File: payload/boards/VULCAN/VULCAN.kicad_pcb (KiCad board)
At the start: 2 copper layers, 63.5 x 101.6 mm, 78 parts, among them IC1 LT1001CS8#PBF, J1 XT60PW-M, J2 POWER, J3 I2C, J4 Serial, J5 SPI, J6 GPIO, J7 Screw_Terminal_01x06, J8 Screw_Terminal_01x06, U1 AZ1117IH-5.0TRG1, U2 DS18B20, U3 MAX31850KATB+T, U4 AP63357, U5 DEV-16771, U6 MAX31850KATB+T, U7 MAX31850KATB+T, U8 MAX31850KATB+T

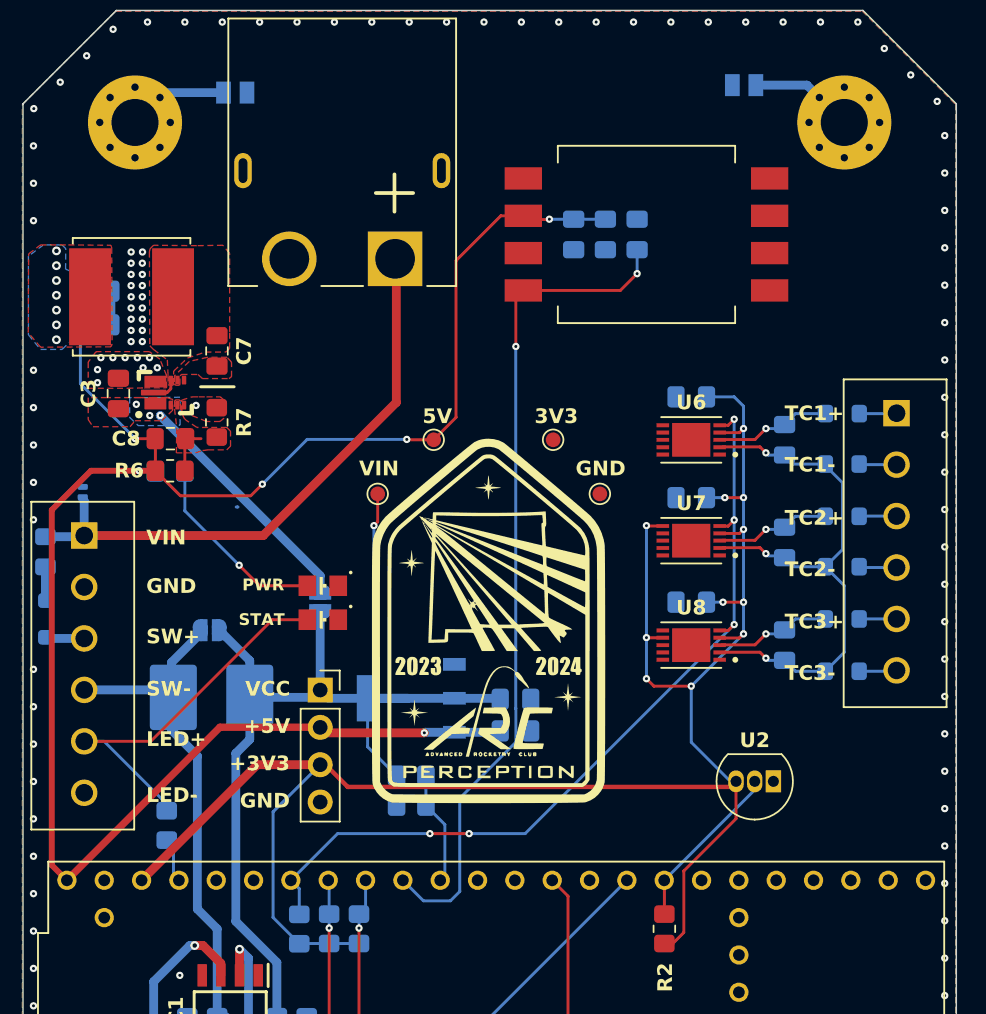
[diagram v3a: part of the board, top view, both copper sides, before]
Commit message: added ESD to TCs
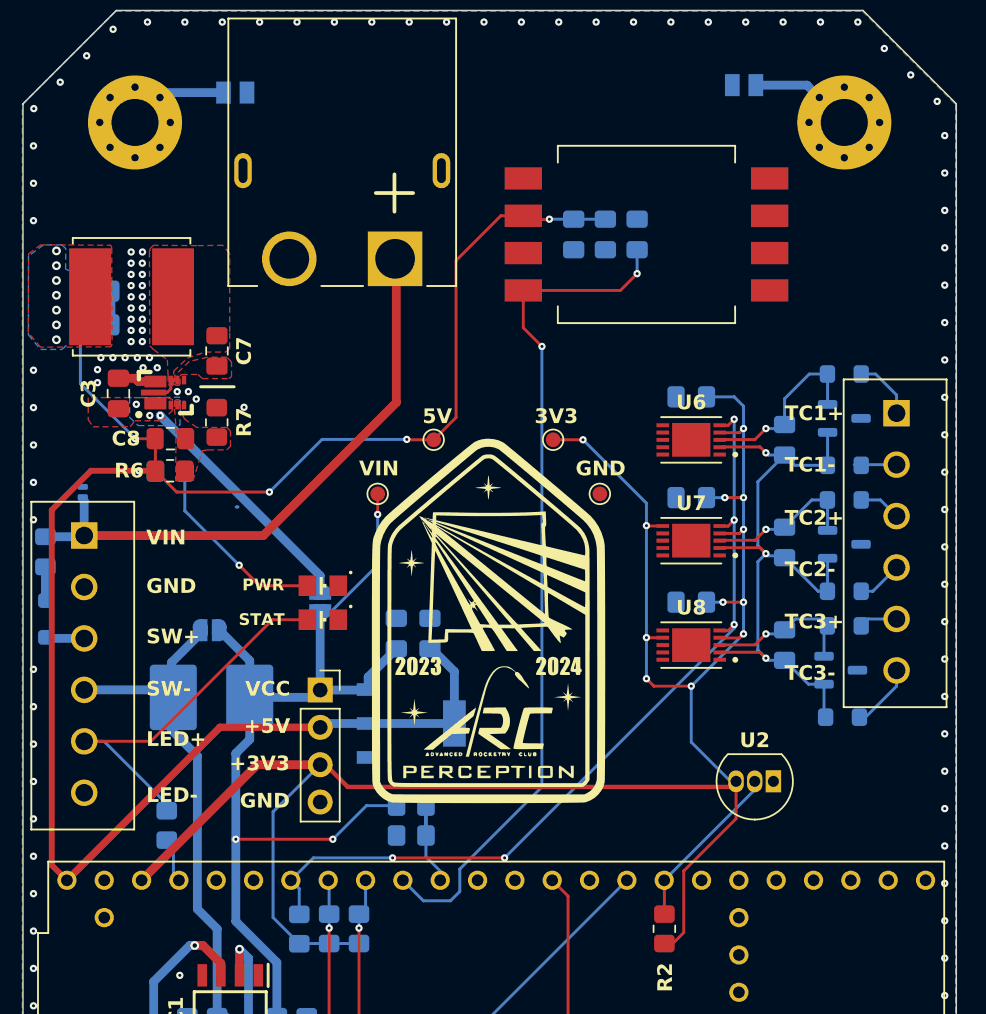
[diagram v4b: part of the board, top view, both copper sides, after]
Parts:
- added D11: NUP2105LT1G, Package_TO_SOT_SMD:SOT-23-3, B.Cu at (208.3, 73.5)
- added D6: NUP2105LT1G, Package_TO_SOT_SMD:SOT-23-3, B.Cu at (208.3, 82.0)
- added D7: NUP2105LT1G, Package_TO_SOT_SMD:SOT-23-3, B.Cu at (208.0, 90.6)
- FB1, FB2, FB3, FB4, FB5, FB6: value 2508056017Y2 -> BLM21SP471BH1D
- R12, R13: value R -> 4.7k
- TP3: value +3.3V -> +3V3
- U3: value MAX31850KATB+T -> MPXV7002DP
- moved C2 10.5 mm to (177.8, 88.1), turned to 90 degrees
- moved C1 7.34 mm to (180.1, 88.1), turned to 90 degrees
- moved FB6 3.12 mm to (208.2, 93.8)
- moved FB1 2.70 mm to (208.3, 70.5)
- moved R10 2.03 mm to (178.8, 101.9)
- moved R9 2.03 mm to (178.8, 99.8)
- moved U1 1.71 mm to (178.8, 94.2), turned to 90 degrees
- moved FB4 1.68 mm to (208.3, 85.2)
- moved FB3 1.12 mm to (208.3, 79.0)
- moved FB5 0.49 mm to (208.3, 87.6)
- moved FB2 0.17 mm to (208.3, 76.7)
- renumbered C13 to C10, C9 to C11, C11 to C12, C10 to C13, C12 to C9
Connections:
- C1 pad 1: /VCC -> /+5V
- C2 pad 1: /+5V -> /VCC
- TP3 pad 1: /+3.3V -> +3V3
- U1 pad 2: /VCC -> /+5V
- U1 pad 3: /+5V -> /VCC
- U5 pad 14: /FAN -> unconnected-(U5-A0-Pad14)
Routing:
- net +3V3: track 132.2 -> 141.8 mm, vias 11 -> 12
- net /T-: track 38.6 -> 45.9 mm
- net /VCC: track 72.4 -> 66.7 mm, vias 1 -> 3
- net /T1: track 7.40 -> 11.8 mm
- net Net-(U4-FB): track 3.17 -> 0.00 mm
- net Net-(JP3-A): track 6.86 -> 3.99 mm
- net /T2: track 7.39 -> 10.1 mm
- net GND: track 2.42 -> 5.02 mm, vias 145 -> 148
- net /+5V: track 126.7 -> 128.9 mm, vias 13 -> 12
- net /T3: track 7.39 -> 9.56 mm
- net Net-(J8-Pin_6): track 2.87 -> 4.47 mm
- net Net-(J8-Pin_1): track 2.88 -> 4.24 mm
- net /PITOT: track 57.5 -> 58.3 mm
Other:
- board text added: "Advanced Rocketry Club"
- board text added: "v1.0"

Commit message: updates
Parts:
- removed D11, D6, D7: NUP2105LT1G, Package_TO_SOT_SMD:SOT-23-3
- removed FB1, FB2, FB3, FB4, FB5, FB6: BLM21SP471BH1D, PCM_Ferrite_SMD_AKL:Ferrite_0805_2012Metric_Pad1.05x1.20mm_BigPads
- R2: moved to B.Cu
- moved R2 7.11 mm to (196.0, 101.1), turned to -90 degrees
- moved C14 6.90 mm to (204.2, 74.7), turned to -90 degrees
- moved C15 6.90 mm to (204.2, 88.7), turned to -90 degrees
- moved C16 6.90 mm to (204.2, 81.6), turned to -90 degrees
- moved C11 5.09 mm to (209.3, 74.7)
- moved C12 5.09 mm to (209.3, 81.7)
- moved C13 5.09 mm to (209.3, 88.6)
- moved U2 2.29 mm to (181.1, 94.2)
- moved C1 2.03 mm to (182.1, 88.1)
- moved C8 2.03 mm to (179.8, 88.1)
- moved TP2 0.51 mm to (179.8, 74.9)
- moved JP3 0.51 mm to (166.8, 50.9)
- renumbered C3 to C2, C5 to C3, C6 to C4, C4 to C5, C7 to C6, C8 to C7, C2 to C8, D2 to D1, D1 to D2, U2 to U1, U1 to U2
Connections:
- D1 pad A: /LED_GRN_RES -> /LED_GRN
- J7 pad 5: /LED_GRN_RES -> /LED_GRN
- J8 pad 1: Net-(J8-Pin_1) -> /T1
- J8 pad 2: Net-(J8-Pin_2) -> /T-
- J8 pad 3: Net-(J8-Pin_3) -> /T2
- J8 pad 4: Net-(J8-Pin_4) -> /T-
- J8 pad 5: Net-(J8-Pin_5) -> /T3
- J8 pad 6: Net-(J8-Pin_6) -> /T-
- R11 pad 1: /LED_GRN_RES -> /LED_GRN
- R11 pad 2: /LED_GRN -> Net-(U5-A9)
- U5 pad 23: /LED_GRN -> Net-(U5-A9)
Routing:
- net /LED_GRN_RES: track 26.0 -> 0.00 mm
- net /LED_GRN: track 1.91 -> 26.0 mm
- net /VCC: track 66.7 -> 50.8 mm
- net /VBAT_SW: track 35.8 -> 27.0 mm
- net /T-: track 45.9 -> 54.5 mm
- net Net-(J8-Pin_6): track 4.47 -> 0.00 mm
- net Net-(J8-Pin_1): track 4.24 -> 0.00 mm
- net +3V3: track 141.8 -> 138.5 mm, vias 12 -> 7
- net Net-(J8-Pin_4): track 3.07 -> 0.00 mm
- net /T3: track 9.56 -> 12.6 mm
- net Net-(J8-Pin_2): track 2.88 -> 0.00 mm
- net Net-(J8-Pin_3): track 2.86 -> 0.00 mm
- net GND: track 5.02 -> 7.62 mm, vias 148 -> 150
- net Net-(J8-Pin_5): track 2.60 -> 0.00 mm
- net /+5V: track 128.9 -> 131.4 mm
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- added copper zone on B.Cu, net /VBAT_SW
- added copper zone on B.Cu, net /VCC
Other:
- board text added: "Backup LDO"
- board text added: "CR2032 / RTC"
- board text added: "PWR 6V-16.8V"
- board text added: "STATUS"
- board text added: "Thermocouples (Type-K)"
- board text added: "VULCAN v1.0 Advanced Rocketry Club Luca Beretta 05/2024"
- board text removed: "Advanced Rocketry Club"
- board text removed: "CR2032"
- board text removed: "Designed by Luca Beretta"
- board text removed: "PWR 12.6V"
- board text removed: "STAT"
- board text removed: "Thermocouple Inputs"

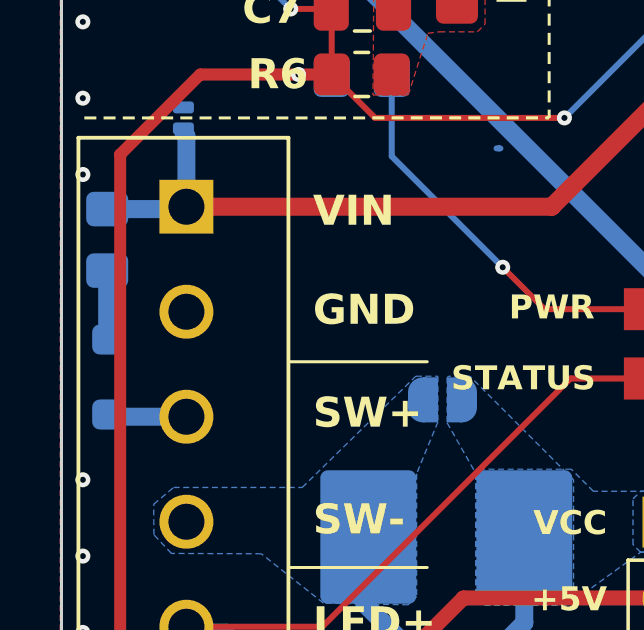
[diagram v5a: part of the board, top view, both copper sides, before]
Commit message: updated BOM
distributor and manufacturer part number
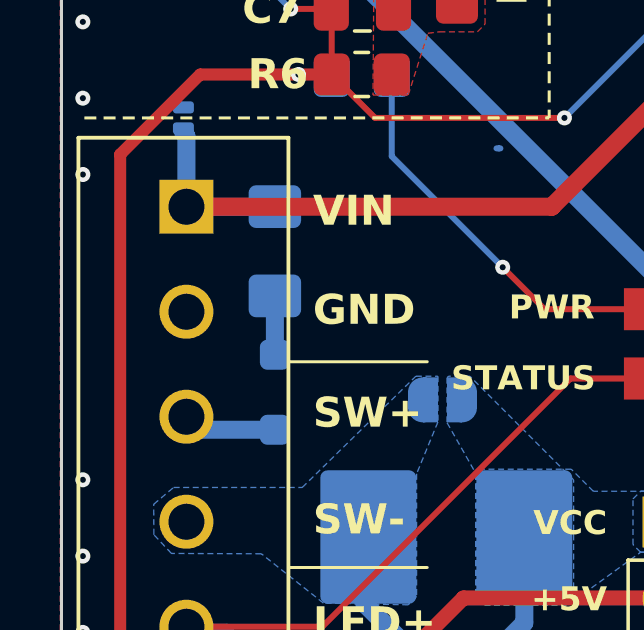
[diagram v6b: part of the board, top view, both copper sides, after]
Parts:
- F1: value 1.5A -> 500mA; footprint Fuse:Fuse_0805_2012Metric_Pad1.15x1.40mm_HandSolder -> Fuse:Fuse_1206_3216Metric_Pad1.42x1.75mm_HandSolder
- R5, R8: value 5K -> 5.1K
- U1: value DS18B20 -> DS18B20+
- U4: value AP63357 -> AP63357QZV-7
- U5: value DEV-16771 -> Teensy 4.1
- moved D4 5.61 mm to (159.5, 87.6)
- moved F1 5.60 mm to (159.5, 82.9)
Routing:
- net /VBAT_RP: track 2.56 -> 3.13 mm
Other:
- board text added: "500mA"
